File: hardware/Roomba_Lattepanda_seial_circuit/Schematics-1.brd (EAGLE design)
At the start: 20 x 25.4 mm, 5 parts

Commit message: local server
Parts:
- removed D1: U57X32, led:U57X32
- removed JP10, JP6: (no value), adafruit:1X01
- added JP1, JP2, JP3, JP4, JP5: (no value), adafruit:1X01-CLEANBIG
- added LD2: (no value), led:DUOLED-C-5MM
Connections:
- new net N$2: JP1.1, JP4.1
- new net N$5: JP5.1, LD2.AX
- new net N$7: JP2.1, LD2.C
- net N$4: now also JP3.1, LD2.AR; no longer D1.A
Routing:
- net N$5: track 0.00 -> 11.4 mm
- net N$7: track 0.00 -> 7.62 mm
- net N$2: track 0.00 -> 5.39 mm
- net N$4: track 23.7 -> 28.2 mm
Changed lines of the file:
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@@
 </autorouter>
 <elements>
-<element name="JP10" library="adafruit" package="1X01" value="" x="5.08" y="7.62"/>
-<element name="JP6" library="adafruit" package="1X01" value="" x="5.08" y="17.78"/>
 <element name="LD1" library="led" package="DUOLED-C-5MM" value="" x="16.51" y="20.32" rot="R90"/>
-<element name="D1" library="led" package="U57X32" value="U57X32" x="2.54" y="3.81" rot="R270"/>
 <element name="D2" library="led" package="U57X32" value="U57X32" x="2.54" y="21.59" rot="R270"/>
+<element name="JP1" library="adafruit" package="1X01-CLEANBIG" value="" x="5.08" y="17.78"/>
+<element name="LD2" library="led" package="DUOLED-C-5MM" value="" x="16.51" y="5.08" rot="R90"/>
+<element name="JP2" library="adafruit" package="1X01-CLEANBIG" value="" x="8.89" y="5.08"/>
+<element name="JP4" library="adafruit" package="1X01-CLEANBIG" value="" x="8.89" y="13.97"/>
+<element name="JP3" library="adafruit" package="1X01-CLEANBIG" value="" x="2.54" y="5.08"/>
+<element name="JP5" library="adafruit" package="1X01-CLEANBIG" value="" x="5.08" y="2.54"/>
 </elements>
 <signals>
 <signal name="N$4">
-<contactref element="D1" pad="A"/>
 <contactref element="LD1" pad="AX"/>
-<wire x1="2.54" y1="5.08" x2="7.62" y2="5.08" width="1.016" layer="16"/>
-<wire x1="7.62" y1="5.08" x2="10.16" y2="7.62" width="1.016" layer="16"/>
-<wire x1="10.16" y1="7.62" x2="10.16" y2="15.24" width="1.016" layer="16"/>
-<wire x1="10.16" y1="15.24" x2="12.7" y2="17.78" width="1.016" layer="16"/>
-<wire x1="12.7" y1="17.78" x2="16.51" y2="17.78" width="1.016" layer="16"/>
+<wire x1="12.7" y1="7.62" x2="12.7" y2="16.51" width="1.016" layer="16"/>
+<wire x1="12.7" y1="16.51" x2="13.97" y2="17.78" width="1.016" layer="16"/>
+<wire x1="13.97" y1="17.78" x2="16.51" y2="17.78" width="1.016" layer="16"/>
+<contactref element="LD2" pad="AR"/>
+<wire x1="16.51" y1="7.62" x2="12.7" y2="7.62" width="0.8128" layer="16"/>
+<wire x1="12.7" y1="7.62" x2="7.62" y2="7.62" width="0.8128" layer="16"/>
+<wire x1="7.62" y1="7.62" x2="5.08" y2="5.08" width="0.8128" layer="16"/>
+<contactref element="JP3" pad="1"/>
+<wire x1="2.54" y1="5.08" x2="5.08" y2="5.08" width="0.8128" layer="16"/>
 </signal>
 <signal name="N$1">
@@
 <wire x1="2.54" y1="20.32" x2="16.51" y2="20.32" width="1.016" layer="16"/>
 </signal>
+<signal name="N$5">
+<contactref element="LD2" pad="AX"/>
+<contactref element="JP5" pad="1"/>
+<wire x1="5.08" y1="2.54" x2="16.51" y2="2.54" width="0.8128" layer="16"/>
+</signal>
+<signal name="N$2">
+<contactref element="JP1" pad="1"/>
+<wire x1="5.08" y1="17.78" x2="8.89" y2="13.97" width="0.8128" layer="16"/>
+<contactref element="JP4" pad="1"/>
+<wire x1="8.89" y1="13.97" x2="5.08" y2="17.78" width="0" layer="19" extent="1-1"/>
+</signal>
+<signal name="N$7">
+<contactref element="LD2" pad="C"/>
+<contactref element="JP2" pad="1"/>
+<wire x1="8.89" y1="5.08" x2="16.51" y2="5.08" width="0.8128" layer="16"/>
+</signal>
 </signals>

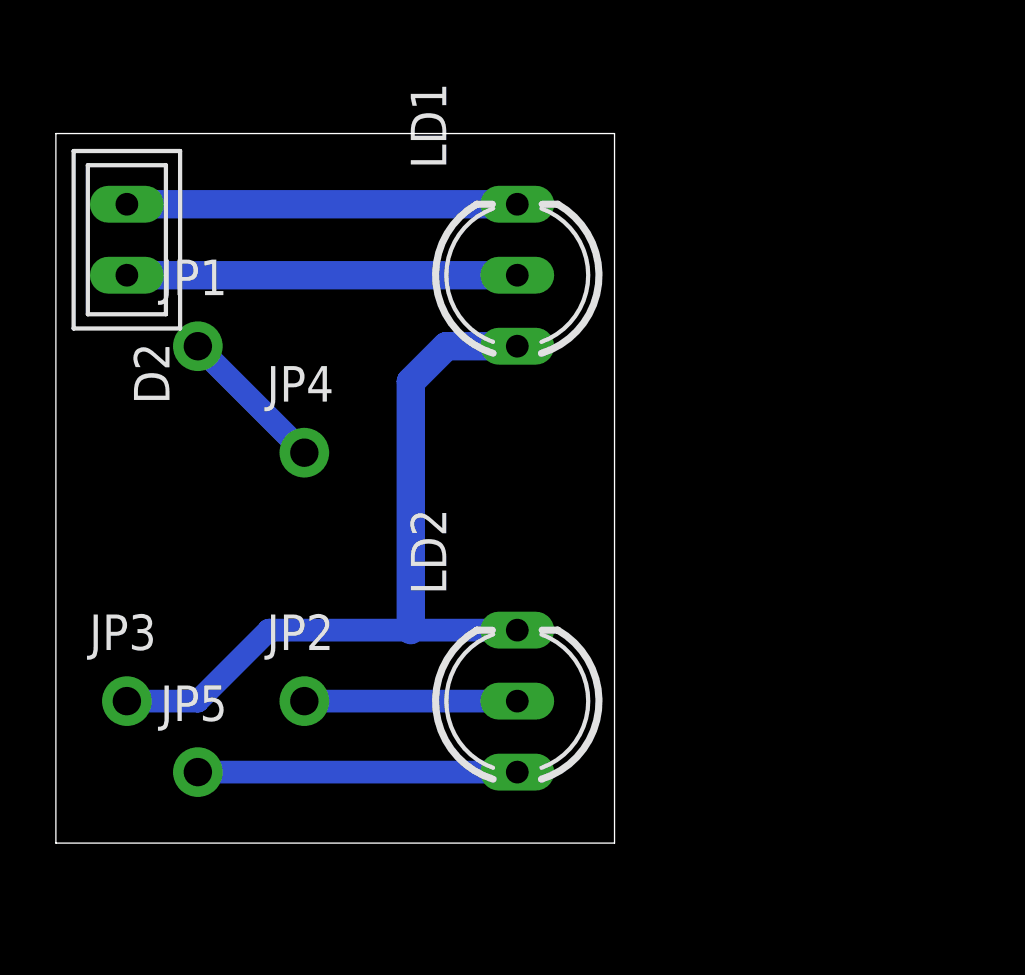
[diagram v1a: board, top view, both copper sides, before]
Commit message: add new board/ add perfect stitch helper
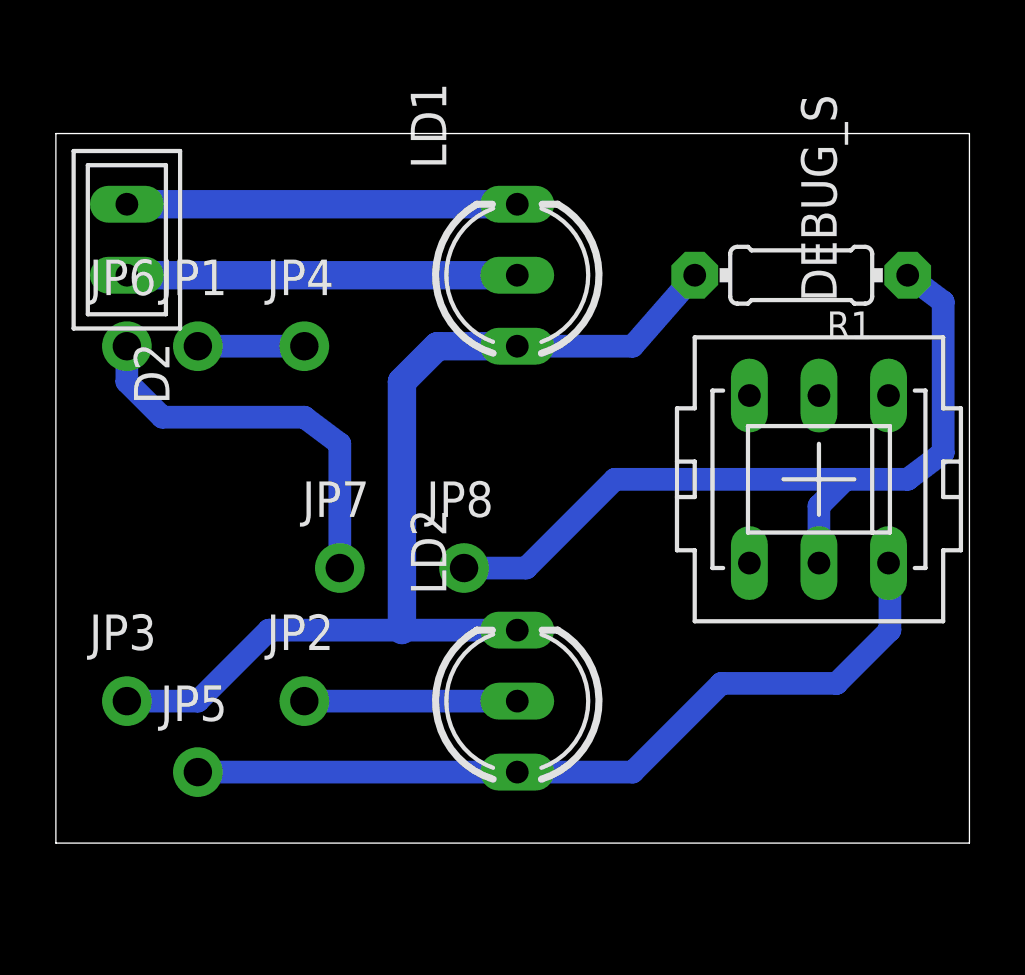
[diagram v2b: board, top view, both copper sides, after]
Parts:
- added DEBUG_S: PVA2R, switch-misc:PVA2R
- added JP6, JP7, JP8: (no value), adafruit:1X01-CLEANBIG
- added R1: (no value), adafruit:0204/7
- moved JP4 3.81 mm to (8.89, 17.8)
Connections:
- new net N$6: DEBUG_S.2, JP8.1, R1.1
- new net N$8: JP6.1, JP7.1
- net N$4: now also R1.2
- net N$5: now also DEBUG_S.3
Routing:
- net N$6: track 0.00 -> 29.2 mm
- net N$5: track 11.4 -> 29.3 mm
- net N$8: track 0.00 -> 14.2 mm
- net N$4: track 28.2 -> 36.1 mm
- net N$2: track 5.39 -> 3.81 mm
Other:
- board size 20 x 25.4 mm -> 32.7 x 25.4 mm
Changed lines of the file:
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@@
 <setting verticaltext="up"/>
 </settings>
-<grid distance="0.05" unitdist="inch" unit="inch" style="lines" multiple="1" display="no" altdistance="0.025" altunitdist="inch" altunit="inch"/>
+<grid distance="0.0125" unitdist="inch" unit="inch" style="dots" multiple="1" display="yes" altdistance="0.0125" altunitdist="inch" altunit="inch"/>
 <layers>
 <layer number="1" name="Top" color="4" fill="1" visible="yes" active="yes"/>
@@
 <board>
 <plain>
-<wire x1="0" y1="0" x2="19.99" y2="0" width="0" layer="20"/>
-<wire x1="19.99" y1="0" x2="19.99" y2="25.39" width="0" layer="20"/>
-<wire x1="19.99" y1="25.39" x2="0" y2="25.39" width="0" layer="20"/>
+<wire x1="0" y1="0" x2="32.69" y2="0" width="0" layer="20"/>
+<wire x1="32.69" y1="0" x2="32.69" y2="25.39" width="0" layer="20"/>
+<wire x1="32.69" y1="25.39" x2="0" y2="25.39" width="0" layer="20"/>
 <wire x1="0" y1="25.39" x2="0" y2="0" width="0" layer="20"/>
 </plain>
@@
 <element name="LD2" library="led" package="DUOLED-C-5MM" value="" x="16.51" y="5.08" rot="R90"/>
 <element name="JP2" library="adafruit" package="1X01-CLEANBIG" value="" x="8.89" y="5.08"/>
-<element name="JP4" library="adafruit" package="1X01-CLEANBIG" value="" x="8.89" y="13.97"/>
+<element name="JP4" library="adafruit" package="1X01-CLEANBIG" value="" x="8.89" y="17.78"/>
 <element name="JP3" library="adafruit" package="1X01-CLEANBIG" value="" x="2.54" y="5.08"/>
 <element name="JP5" library="adafruit" package="1X01-CLEANBIG" value="" x="5.08" y="2.54"/>
+<element name="R1" library="adafruit" package="0204/7" value="" x="26.67" y="20.32" rot="R180"/>
+<element name="DEBUG_S" library="switch-misc" package="PVA2R" value="PVA2R" x="27.305" y="13.0175" rot="R90"/>
+<element name="JP6" library="adafruit" package="1X01-CLEANBIG" value="" x="2.54" y="17.78"/>
+<element name="JP7" library="adafruit" package="1X01-CLEANBIG" value="" x="10.16" y="9.8425"/>
+<element name="JP8" library="adafruit" package="1X01-CLEANBIG" value="" x="14.605" y="9.8425"/>
 </elements>
 <signals>
 <signal name="N$4">
 <contactref element="LD1" pad="AX"/>
-<wire x1="12.7" y1="7.62" x2="12.7" y2="16.51" width="1.016" layer="16"/>
-<wire x1="12.7" y1="16.51" x2="13.97" y2="17.78" width="1.016" layer="16"/>
-<wire x1="13.97" y1="17.78" x2="16.51" y2="17.78" width="1.016" layer="16"/>
+<wire x1="12.3825" y1="7.62" x2="12.3825" y2="16.51" width="1.016" layer="16"/>
+<wire x1="12.3825" y1="16.51" x2="13.6525" y2="17.78" width="1.016" layer="16"/>
+<wire x1="13.6525" y1="17.78" x2="16.51" y2="17.78" width="1.016" layer="16"/>
 <contactref element="LD2" pad="AR"/>
-<wire x1="16.51" y1="7.62" x2="12.7" y2="7.62" width="0.8128" layer="16"/>
-<wire x1="12.7" y1="7.62" x2="7.62" y2="7.62" width="0.8128" layer="16"/>
+<wire x1="16.51" y1="7.62" x2="12.3825" y2="7.62" width="0.8128" layer="16"/>
+<wire x1="12.3825" y1="7.62" x2="7.62" y2="7.62" width="0.8128" layer="16"/>
 <wire x1="7.62" y1="7.62" x2="5.08" y2="5.08" width="0.8128" layer="16"/>
 <contactref element="JP3" pad="1"/>
 <wire x1="2.54" y1="5.08" x2="5.08" y2="5.08" width="0.8128" layer="16"/>
+<contactref element="R1" pad="2"/>
+<wire x1="16.51" y1="17.78" x2="20.6375" y2="17.78" width="0.8128" layer="16"/>
+<wire x1="20.6375" y1="17.78" x2="22.86" y2="20.32" width="0.8128" layer="16"/>
 </signal>
 <signal name="N$1">
@@
 <contactref element="JP5" pad="1"/>
 <wire x1="5.08" y1="2.54" x2="16.51" y2="2.54" width="0.8128" layer="16"/>
+<wire x1="16.51" y1="2.54" x2="20.6375" y2="2.54" width="0.8128" layer="16"/>
+<contactref element="DEBUG_S" pad="3"/>
+<wire x1="20.6375" y1="2.54" x2="23.8125" y2="5.715" width="0.8128" layer="16"/>
+<wire x1="23.8125" y1="5.715" x2="27.94" y2="5.715" width="0.8128" layer="16"/>
+<wire x1="27.94" y1="5.715" x2="29.845" y2="7.62" width="0.8128" layer="16"/>
+<wire x1="29.845" y1="7.62" x2="29.845" y2="9.9695" width="0.8128" layer="16"/>
+<wire x1="29.845" y1="9.9695" x2="29.7942" y2="10.0203" width="0.8128" layer="16"/>
 </signal>
 <signal name="N$2">
 <contactref element="JP1" pad="1"/>
-<wire x1="5.08" y1="17.78" x2="8.89" y2="13.97" width="0.8128" layer="16"/>
+<wire x1="5.08" y1="17.78" x2="8.89" y2="17.78" width="0.8128" layer="16"/>
 <contactref element="JP4" pad="1"/>
-<wire x1="8.89" y1="13.97" x2="5.08" y2="17.78" width="0" layer="19" extent="1-1"/>
 </signal>
 <signal name="N$7">
@@
 <wire x1="8.89" y1="5.08" x2="16.51" y2="5.08" width="0.8128" layer="16"/>
 </signal>
+<signal name="N$6">
+<contactref element="R1" pad="1"/>
+<contactref element="DEBUG_S" pad="2"/>
+<wire x1="27.305" y1="10.0203" x2="27.305" y2="12.065" width="0.8128" layer="16"/>
+<wire x1="27.305" y1="12.065" x2="28.2575" y2="13.0175" width="0.8128" layer="16"/>
+<wire x1="28.2575" y1="13.0175" x2="30.48" y2="13.0175" width="0.8128" layer="16"/>
+<wire x1="30.48" y1="13.0175" x2="31.75" y2="13.97" width="0.8128" layer="16"/>
+<wire x1="31.75" y1="13.97" x2="31.75" y2="19.3675" width="0.8128" layer="16"/>
+<wire x1="30.48" y1="20.32" x2="31.75" y2="19.3675" width="0.8128" layer="16"/>
+<contactref element="JP8" pad="1"/>
+<wire x1="14.605" y1="9.8425" x2="16.8275" y2="9.8425" width="0.8128" layer="16"/>
+<wire x1="16.8275" y1="9.8425" x2="20.0025" y2="13.0175" width="0.8128" layer="16"/>
+<wire x1="20.0025" y1="13.0175" x2="28.2575" y2="13.0175" width="0.8128" layer="16"/>
+</signal>
+<signal name="N$8">
+<contactref element="JP6" pad="1"/>
+<contactref element="JP7" pad="1"/>
+<wire x1="2.54" y1="17.78" x2="2.54" y2="16.51" width="0.8128" layer="16"/>
+<wire x1="2.54" y1="16.51" x2="3.81" y2="15.24" width="0.8128" layer="16"/>
+<wire x1="3.81" y1="15.24" x2="8.89" y2="15.24" width="0.8128" layer="16"/>
+<wire x1="8.89" y1="15.24" x2="10.16" y2="14.2875" width="0.8128" layer="16"/>
+<wire x1="10.16" y1="14.2875" x2="10.16" y2="9.8425" width="0.8128" layer="16"/>
+</signal>
 </signals>
